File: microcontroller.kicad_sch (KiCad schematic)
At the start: 37 parts, among them J1 Conn_01x05_Pin, J2 HRO_TYPE-C-31-M-12, J3 Conn_01x04, J4 Conn_01x06, J5 Conn_01x06, J6 Conn_01x04, J7 Conn_01x04, SW1 SKRPANE010, SW2 EC11E18244AU, U1 USBLC6-2SC6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

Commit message: Add buzzer, fix some erc
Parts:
- added BZ1: MLT-7525, Library:MLT-7525, symbol libchickenstick:Buzzer
- added D12: 1N4148, APRLPrints:SOD-323, symbol Device:D_Small
- added Q3: 2N7002, Package_TO_SOT_SMD:SOT-23, symbol Transistor_FET:2N7002
- added R19: 10k, APRLPrints:R_0603, symbol Device:R_Small_US
- added R20: 100R, APRLPrints:R_0603, symbol Device:R_Small_US
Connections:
- net +VUSB: now also BZ1.1 (+), D12.1 (K)
- net GND: now also Q3.2 (S), R19.2
- net BUZZER: now reaches U2.29 (PA8)
- net BUZZER: now also R20.1
- new net: Q3.1 (G), R19.1, R20.2
- new net: BZ1.2 (-), D12.2 (A), Q3.3 (D)
- new net: BZ1.3, BZ1.4
- no-connect marks 7 -> 6
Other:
- note added: "Wilson's Buzzer (He did not ask for this)"

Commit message: Remove big SS14 diodes
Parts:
- removed D1: SS14, Diode_SMD:D_SMA, symbol Diode:SS14
- D1: renamed from D5; value SS14 -> MM3Z10VT1G; footprint Diode_SMD:D_SMA -> APRLPrints:SOD-323
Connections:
- net +VUSB: now also F1.2
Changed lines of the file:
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@@
 	)
 	(junction
-		(at 229.87 33.02)
+		(at 97.79 49.53)
 		(diameter 0)
 		(color 0 0 0 0)
 	)
 	(junction
-		(at 97.79 49.53)
+		(at 106.68 38.1)
 		(diameter 0)
 		(color 0 0 0 0)
 	)
 	(junction
-		(at 106.68 38.1)
+		(at 224.79 33.02)
 		(diameter 0)
 		(color 0 0 0 0)
@@
 	(wire
 		(pts
-			(xy 233.68 31.75) (xy 233.68 33.02)
+			(xy 229.87 31.75) (xy 229.87 33.02)
 		)
 		(stroke
@@
 	(wire
 		(pts
+			(xy 224.79 33.02) (xy 229.87 33.02)
+		)
+		(stroke
+			(width 0)
+			(type default)
+		)
+	)
+	(wire
+		(pts
 			(xy 229.87 119.38) (xy 229.87 118.11)
 		)
@@
 	(wire
 		(pts
-			(xy 214.63 33.02) (xy 220.98 33.02)
+			(xy 214.63 33.02) (xy 224.79 33.02)
 		)
 		(stroke
@@
 	(wire
 		(pts
-			(xy 229.87 31.75) (xy 229.87 33.02)
+			(xy 224.79 31.75) (xy 224.79 33.02)
 		)
 		(stroke
@@
 	(wire
 		(pts
-			(xy 229.87 33.02) (xy 233.68 33.02)
-		)
-		(stroke
-			(width 0)
-			(type default)
-		)
-	)
-	(wire
-		(pts
 			(xy 137.16 40.64) (xy 137.16 41.91)
 		)
@@
 	(wire
 		(pts
-			(xy 229.87 33.02) (xy 228.6 33.02)
-		)
-		(stroke
-			(width 0)
-			(type default)
-		)
-	)
-	(wire
-		(pts
 			(xy 193.04 127) (xy 193.04 125.73)
 		)
@@
 	(symbol
 		(lib_id "power:VBUS")
-		(at 233.68 31.75 0)
+		(at 229.87 31.75 0)
 		(unit 1)
 		(body_style 1)
@@
 		(fields_autoplaced yes)
 		(property "Reference" "#PWR02"
-			(at 233.68 35.56 0)
+			(at 229.87 35.56 0)
 			(hide yes)
 			(show_name no)
@@
 		)
 		(property "Value" "+VUSB"
-			(at 233.68 26.67 0)
+			(at 229.87 26.67 0)
 			(show_name no)
 			(do_not_autoplace no)
@@
 		)
 		(property "Footprint" ""
-			(at 233.68 31.75 0)
+			(at 229.87 31.75 0)
 			(hide yes)
 			(show_name no)
@@
 		)
 		(property "Datasheet" ""
-			(at 233.68 31.75 0)
+			(at 229.87 31.75 0)
 			(hide yes)
 			(show_name no)
@@
 		)
 		(property "Description" "Power symbol creates a global label with name \"VBUS\""
-			(at 233.68 31.75 0)
+			(at 229.87 31.75 0)
 			(hide yes)
 			(show_name no)
@@
 		(dnp no)
 		(fields_autoplaced yes)
-		(property "Reference" "D5"
+		(property "Reference" "D1"
 			(at 216.8525 96.52 0)
 			(show_name no)
@@
 			)
 		)
-		(property "Value" "SS14"
+		(property "Value" "MM3Z10VT1G"
 			(at 216.8525 99.06 0)
 			(show_name no)
@@
 			)
 		)
-		(property "Footprint" "Diode_SMD:D_SMA"
+		(property "Footprint" "APRLPrints:SOD-323"
 			(at 217.17 107.315 0)
 			(hide yes)
@@
 			)
 		)
-		(property "Datasheet" "https://www.vishay.com/docs/88746/ss12.pdf"
+		(property "Datasheet" "https://www.vishay.com/docs/85764/bzx384.pdf"
 			(at 217.17 102.87 0)
 			(hide yes)
@@
 			)
 		)
-		(property "Description" "40V 1A Schottky Diode, SMA"
+		(property "Description" "300mW Zener Diode, SOD-323"
 			(at 217.17 102.87 0)
 			(hide yes)
@@
 			(project "chickensticks"
 				(path "/ac09718b-d0ae-4ba8-97ca-421d17235641/7fce809c-f583-497b-9755-7d2b61019aef"
-					(reference "D5")
+					(reference "D1")
 					(unit 1)
 				)
@@
 	)
 	(symbol
-		(lib_id "Diode:SS14")
-		(at 224.79 33.02 180)
-		(unit 1)
-		(body_style 1)
-		(exclude_from_sim no)
-		(in_bom yes)
-		(on_board yes)
-		(in_pos_files yes)
-		(dnp no)
-		(fields_autoplaced yes)
-		(property "Reference" "D1"
-			(at 225.1075 26.67 0)
-			(show_name no)
-			(do_not_autoplace no)
-			(effects
-				(font
-					(size 1.27 1.27)
-				)
-			)
-		)
-		(property "Value" "SS14"
-			(at 225.1075 29.21 0)
-			(show_name no)
-			(do_not_autoplace no)
-			(effects
-				(font
-					(size 1.27 1.27)
-				)
-			)
-		)
-		(property "Footprint" "Diode_SMD:D_SMA"
-			(at 224.79 28.575 0)
-			(hide yes)
-			(show_name no)
-			(do_not_autoplace no)
-			(effects
-				(font
-					(size 1.27 1.27)
-				)
-			)
-		)
-		(property "Datasheet" "https://www.vishay.com/docs/88746/ss12.pdf"
-			(at 224.79 33.02 0)
-			(hide yes)
-			(show_name no)
-			(do_not_autoplace no)
-			(effects
-				(font
-					(size 1.27 1.27)
-				)
-			)
-		)
-		(property "Description" "40V 1A Schottky Diode, SMA"
-			(at 224.79 33.02 0)
-			(hide yes)
-			(show_name no)
-			(do_not_autoplace no)
-			(effects
-				(font
-					(size 1.27 1.27)
-				)
-			)
-		)
-		(property "KLC_S3.3" ""
-			(at 224.79 33.02 0)
-			(hide yes)
-			(show_name no)
-			(do_not_autoplace no)
-			(effects
-				(font
-					(size 1.27 1.27)
-				)
-			)
-		)
-		(property "KLC_S4.1" ""
-			(at 224.79 33.02 0)
-			(hide yes)
-			(show_name no)
-			(do_not_autoplace no)
-			(effects
-				(font
-					(size 1.27 1.27)
-				)
-			)
-		)
-		(pin "1"
-		)
-		(pin "2"
-		)
-		(instances
-			(project "chickensticks"
-				(path "/ac09718b-d0ae-4ba8-97ca-421d17235641/7fce809c-f583-497b-9755-7d2b61019aef"
-					(reference "D1")
-					(unit 1)
-				)
-			)
-		)
-	)
-	(symbol
 		(lib_id "power:VBUS")
 		(at 123.19 139.7 0)
@@
 	(symbol
 		(lib_id "power:PWR_FLAG")
-		(at 229.87 31.75 0)
+		(at 224.79 31.75 0)
 		(unit 1)
 		(body_style 1)
@@
 		(fields_autoplaced yes)
 		(property "Reference" "#FLG01"
-			(at 229.87 29.845 0)
+			(at 224.79 29.845 0)
 			(hide yes)
 			(show_name no)
@@
 		)
 		(property "Value" "PWR_FLAG"
-			(at 229.87 26.67 0)
+			(at 224.79 26.67 0)
 			(hide yes)
 			(show_name no)
@@
 		)
 		(property "Footprint" ""
-			(at 229.87 31.75 0)
+			(at 224.79 31.75 0)
 			(hide yes)
 			(show_name no)
@@
 		)
 		(property "Datasheet" ""
-			(at 229.87 31.75 0)
+			(at 224.79 31.75 0)
 			(hide yes)
 			(show_name no)
@@
 		)
 		(property "Description" "Special symbol for telling ERC where power comes from"
-			(at 229.87 31.75 0)
+			(at 224.79 31.75 0)
 			(hide yes)
 			(show_name no)

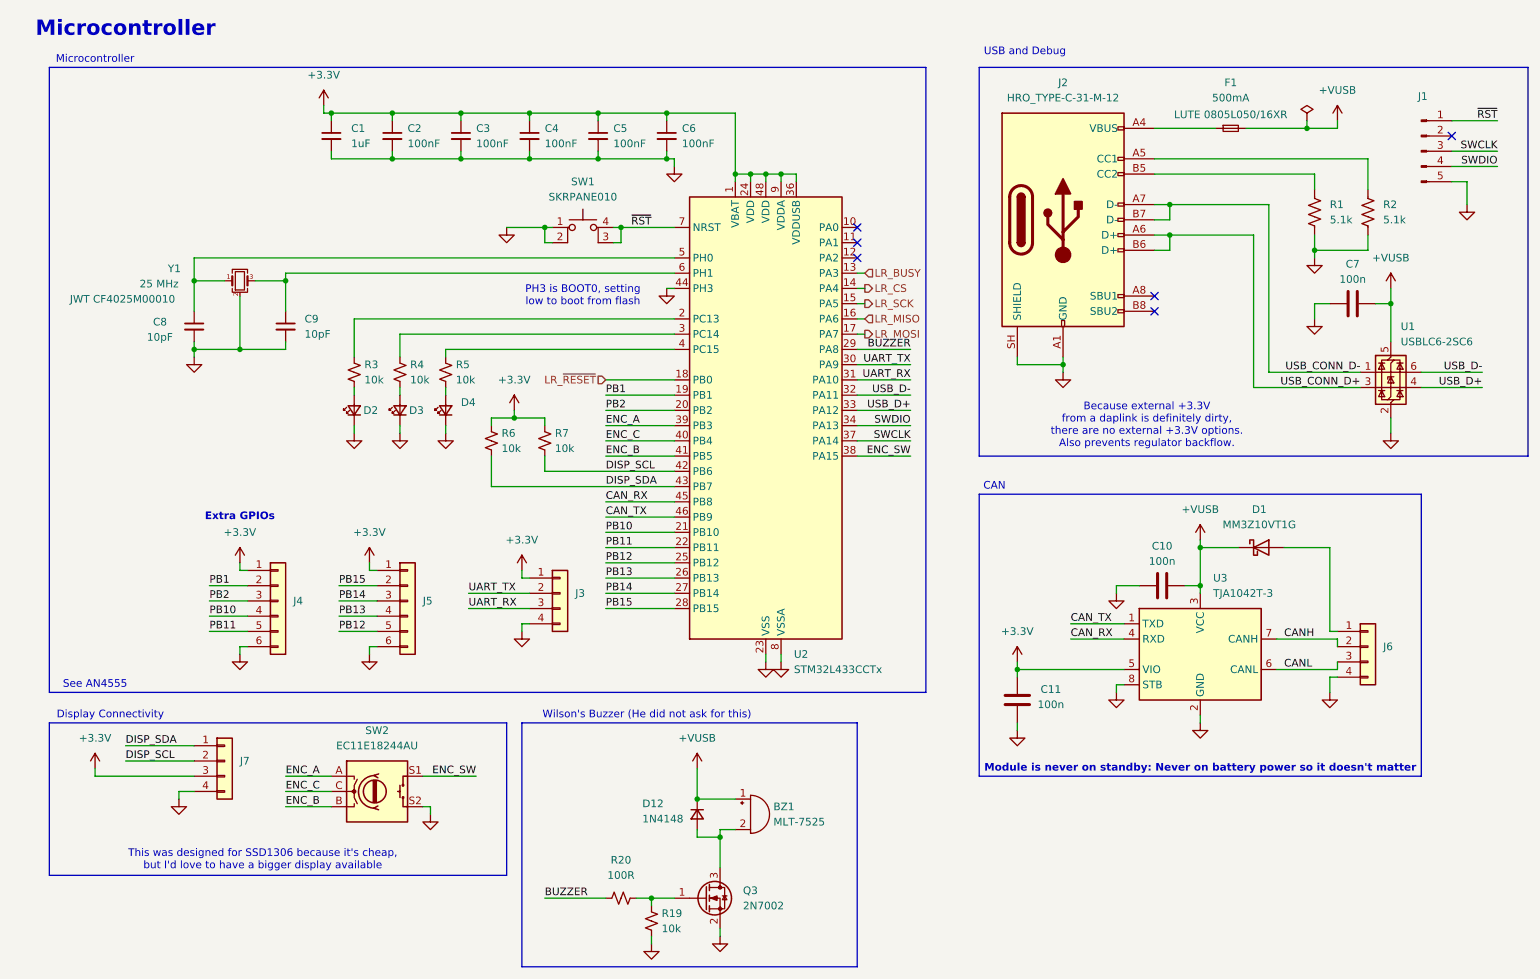
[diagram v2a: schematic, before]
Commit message: Add external 3.3V selector (noise is not real anyway)
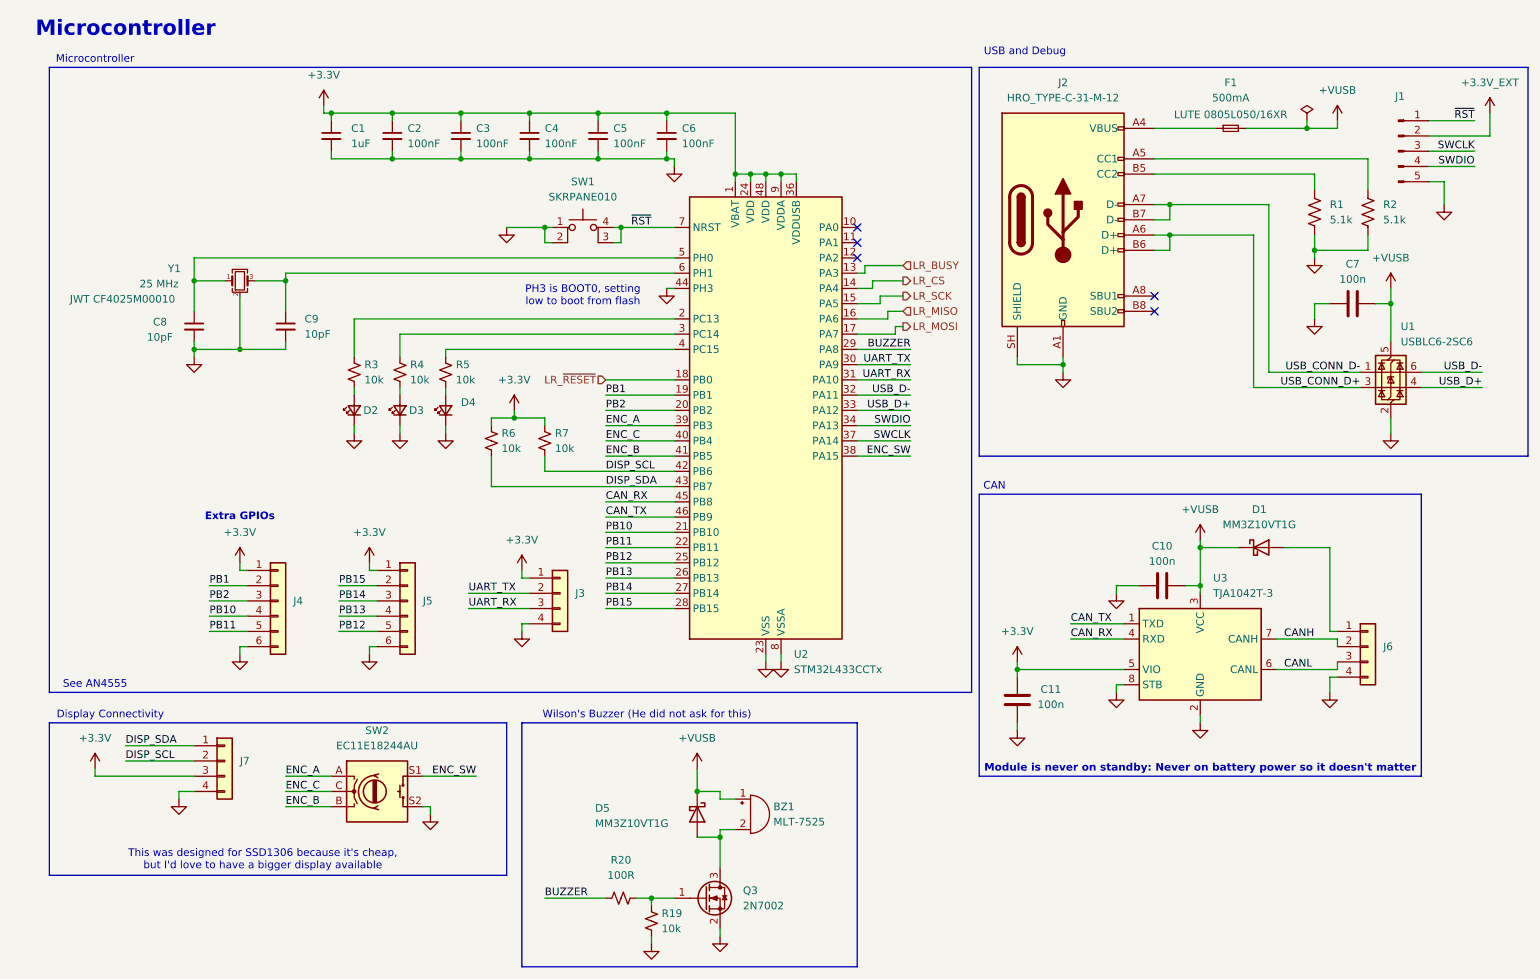
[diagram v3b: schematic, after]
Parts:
- removed D12: 1N4148, APRLPrints:SOD-323, symbol Device:D_Small
- added D5: MM3Z10VT1G, APRLPrints:SOD-323, symbol Diode:SS14
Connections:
- net +VUSB: now also D5.1 (K)
- net at BZ1.2 (-), Q3.3 (D): now also D5.2 (A)
- net +3.3V_EXT: now reaches J1.2 (Pin_2)
- no-connect marks 6 -> 5
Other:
- note removed: "Because external +3.3V from a daplink is definitely dirty, there are no external +3.3V options. Also prevents regulator backflow."
- moved on the sheet: J1
